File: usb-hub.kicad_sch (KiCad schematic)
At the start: 15 parts, among them U302 CH334P, Y900 12Mhz

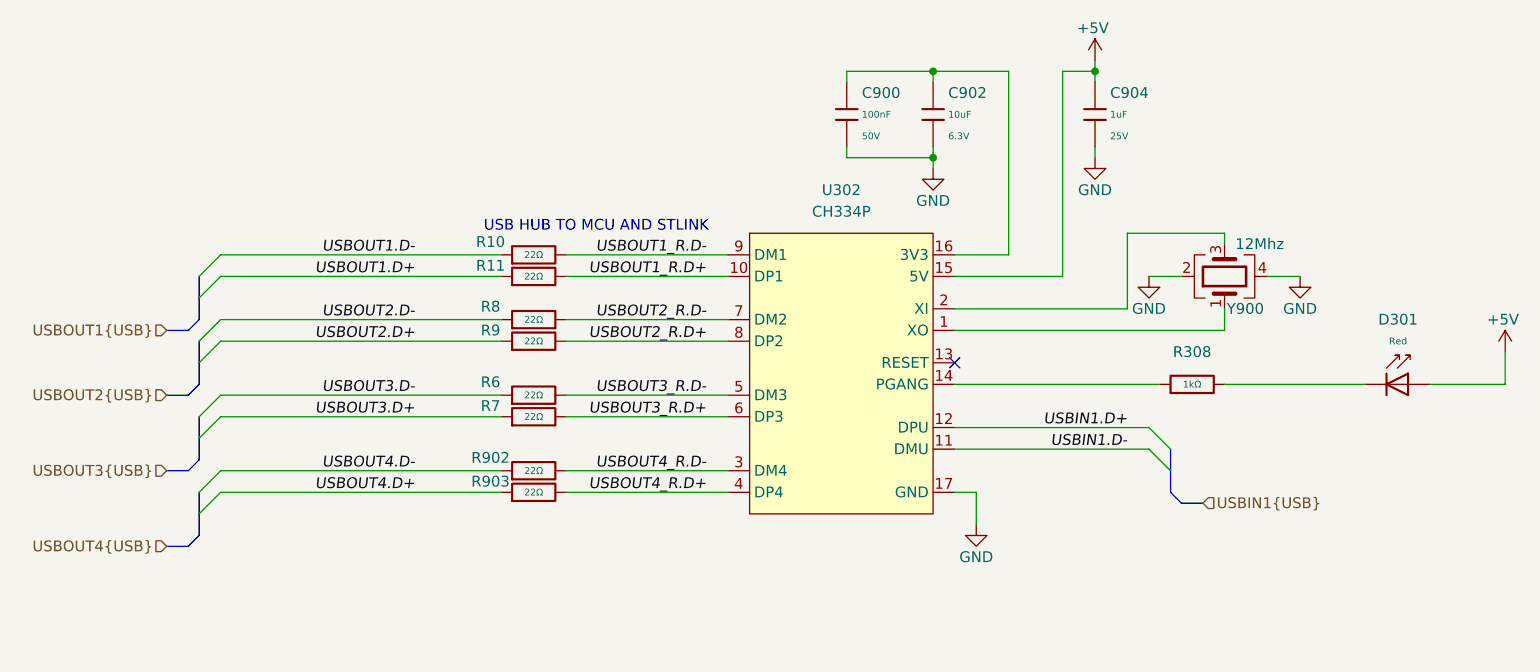
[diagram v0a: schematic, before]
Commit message: [#1] WIP: Change components to ones from the global library, refactor schematic
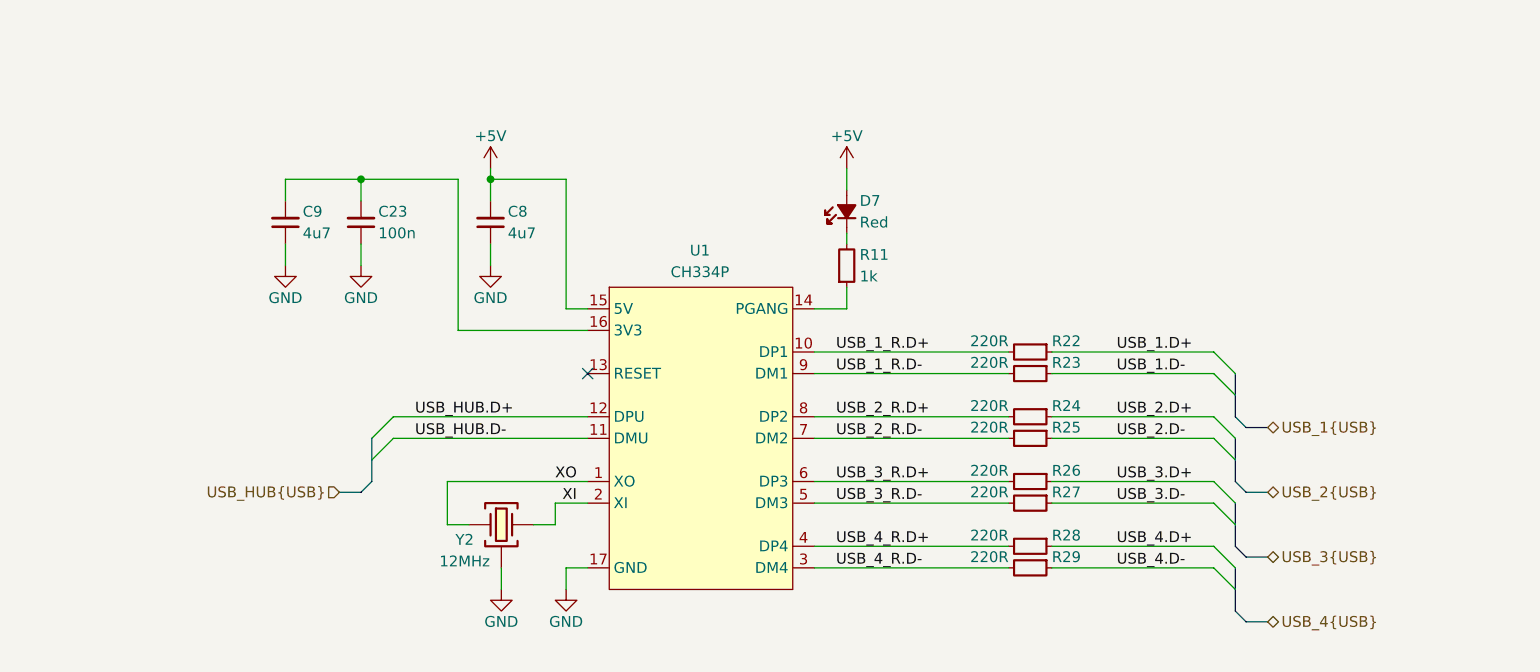
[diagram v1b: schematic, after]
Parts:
- removed C900: 100nF, PCM_JLCPCB:C_0402, symbol PCM_JLCPCB-Capacitors:0402,100nF,(2)
- removed C902: 10uF, PCM_JLCPCB:C_0402, symbol PCM_JLCPCB-Capacitors:0402,10uF
- removed C904: 1uF, PCM_JLCPCB:C_0402, symbol PCM_JLCPCB-Capacitors:0402,1uF
- removed D301: Red, PCM_JLCPCB:D_0603, symbol PCM_JLCPCB-Diodes:LED,0603,Red
- removed R10, R11, R6, R7, R8, R9, R902, R903: 22Ω, PCM_JLCPCB:R_0402, symbol PCM_JLCPCB-Resistors:0402,22Ω
- removed R308: 1kΩ, PCM_JLCPCB:R_0402, symbol PCM_JLCPCB-Resistors:0402,1kΩ
- removed U302: CH334P, Package_DFN_QFN:QFN-16-1EP_3x3mm_P0.5mm_EP1.7x1.7mm, symbol CH334P:CH334P
- removed Y900: 12Mhz, Crystal:Crystal_SMD_3225-4Pin_3.2x2.5mm, symbol Device:Crystal_GND24
- added C23: C-100n-0402, DW-footprints:C_0402_1005Metric, symbol DW-capacitors:C-100n-0402
- added C8, C9: C-4u7-0402, DW-footprints:C_0402_1005Metric, symbol DW-capacitors:C-4u7-0402
- added D7: LED-R-0603_KT-0603R, DW-footprints:LED_0603_1608Metric_R, symbol DW-diodes:LED-R-0603_KT-0603R
- added R11: R-1k-0402, DW-footprints:R_0402_1005Metric, symbol DW-resistors:R-1k-0402
- added R22, R23, R24, R25, R26, R27, R28, R29: R-220r-0402, DW-footprints:R_0402_1005Metric, symbol DW-resistors:R-220r-0402
- added U1: CH334P, DW-footprints:QFN-16-1EP_3x3mm_P0.5mm_EP1.75x1.75mm, symbol DW-ICs:CH334P
- added Y2: X322512MSB4SI, DW-footprints:Crystal_SMD_3225-4Pin_3.2x2.5mm, symbol DW-crystals:Crystal_12MHz_X322512MSB4SI
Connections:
- net +5V: now also C8.2, D7.2 (A), U1.15 (5V)
- net GND: now also C23.1, C8.1, C9.1, U1.17 (GND), Y2.2 (SH), Y2.4 (SH)
- new net: D7.1 (C), R11.2
- new net: R11.1, U1.14 (PGANG)
- new net: C23.2, C9.2, U1.16 (3V3)
- new net USB_1.D+: R22.1
- new net USB_1.D-: R23.1
- new net USB_1_R.D+: R22.2, U1.10 (DP1)
- new net USB_1_R.D-: R23.2, U1.9 (DM1)
- new net USB_2.D+: R24.1
- new net USB_2.D-: R25.1
- new net USB_2_R.D+: R24.2, U1.8 (DP2)
- new net USB_2_R.D-: R25.2, U1.7 (DM2)
- new net USB_3.D+: R26.1
- new net USB_3.D-: R27.1
- new net USB_3_R.D+: R26.2, U1.6 (DP3)
- new net USB_3_R.D-: R27.2, U1.5 (DM3)
- new net USB_4.D+: R28.1
- new net USB_4.D-: R29.1
- new net USB_4_R.D+: R28.2, U1.4 (DP4)
- new net USB_4_R.D-: R29.2, U1.3 (DM4)
- new net USB_HUB.D+: U1.12 (DPU)
- new net USB_HUB.D-: U1.11 (DMU)
- new net XI: U1.2 (XI), Y2.3
- new net XO: U1.1 (XO), Y2.1
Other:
- note removed: "USB HUB TO MCU AND STLINK"

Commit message: [#1] Re-annotate schematic
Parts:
- renumbered C9 to C21, C23 to C22, C8 to C23, D7 to D8, R11 to R26, R22 to R27, R23 to R28, R24 to R29, R25 to R30, R26 to R31, R27 to R32, R28 to R33, R29 to R34, U1 to U5
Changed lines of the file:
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@@
 		(on_board yes)
 		(dnp no)
-		(property "Reference" "D7"
+		(property "Reference" "D8"
 			(at 152.654 77.47 90)
 			(effects
@@
 			(project "cm5-module"
 				(path "/090a8e41-87a8-4fb1-998b-60a2c0dc4cee/4f95f4d3-6409-4bd0-9a25-1272a43f6549"
-					(reference "D7")
+					(reference "D8")
 					(unit 1)
 				)
@@
 		(on_board yes)
 		(dnp no)
-		(property "Reference" "U1"
+		(property "Reference" "U5"
 			(at 133.858 83.312 0)
 			(effects
@@
 			(project ""
 				(path "/090a8e41-87a8-4fb1-998b-60a2c0dc4cee/4f95f4d3-6409-4bd0-9a25-1272a43f6549"
-					(reference "U1")
+					(reference "U5")
 					(unit 1)
 				)
@@
 		(on_board yes)
 		(dnp no)
-		(property "Reference" "R24"
+		(property "Reference" "R29"
 			(at 175.26 101.6 0)
 			(effects
@@
 			(project "cm5-module"
 				(path "/090a8e41-87a8-4fb1-998b-60a2c0dc4cee/4f95f4d3-6409-4bd0-9a25-1272a43f6549"
-					(reference "R24")
+					(reference "R29")
 					(unit 1)
 				)
@@
 		(on_board yes)
 		(dnp no)
-		(property "Reference" "#PWR062"
+		(property "Reference" "#PWR070"
 			(at 85.09 91.44 0)
 			(effects
@@
 			(project "cm5-module"
 				(path "/090a8e41-87a8-4fb1-998b-60a2c0dc4cee/4f95f4d3-6409-4bd0-9a25-1272a43f6549"
-					(reference "#PWR062")
+					(reference "#PWR070")
 					(unit 1)
 				)
@@
 		(on_board yes)
 		(dnp no)
-		(property "Reference" "#PWR058"
+		(property "Reference" "#PWR073"
 			(at 110.49 129.54 0)
 			(effects
@@
 			(project "cm5-module"
 				(path "/090a8e41-87a8-4fb1-998b-60a2c0dc4cee/4f95f4d3-6409-4bd0-9a25-1272a43f6549"
-					(reference "#PWR058")
+					(reference "#PWR073")
 					(unit 1)
 				)
@@
 		(on_board yes)
 		(dnp no)
-		(property "Reference" "#PWR059"
+		(property "Reference" "#PWR071"
 			(at 93.98 91.44 0)
 			(effects
@@
 			(project "cm5-module"
 				(path "/090a8e41-87a8-4fb1-998b-60a2c0dc4cee/4f95f4d3-6409-4bd0-9a25-1272a43f6549"
-					(reference "#PWR059")
+					(reference "#PWR071")
 					(unit 1)
 				)
@@
 		(on_board yes)
 		(dnp no)
-		(property "Reference" "#PWR049"
+		(property "Reference" "#PWR074"
 			(at 118.11 129.54 0)
 			(effects
@@
 			(project "cm5-module"
 				(path "/090a8e41-87a8-4fb1-998b-60a2c0dc4cee/4f95f4d3-6409-4bd0-9a25-1272a43f6549"
-					(reference "#PWR049")
+					(reference "#PWR074")
 					(unit 1)
 				)
@@
 		(on_board yes)
 		(dnp no)
-		(property "Reference" "R23"
+		(property "Reference" "R28"
 			(at 175.26 96.52 0)
 			(effects
@@
 			(project "cm5-module"
 				(path "/090a8e41-87a8-4fb1-998b-60a2c0dc4cee/4f95f4d3-6409-4bd0-9a25-1272a43f6549"
-					(reference "R23")
+					(reference "R28")
 					(unit 1)
 				)
@@
 		(on_board yes)
 		(dnp no)
-		(property "Reference" "R11"
+		(property "Reference" "R26"
 			(at 152.654 83.82 90)
 			(effects
@@
 			(project "cm5-module"
 				(path "/090a8e41-87a8-4fb1-998b-60a2c0dc4cee/4f95f4d3-6409-4bd0-9a25-1272a43f6549"
-					(reference "R11")
+					(reference "R26")
 					(unit 1)
 				)
@@
 		(on_board yes)
 		(dnp no)
-		(property "Reference" "R28"
+		(property "Reference" "R33"
 			(at 175.26 116.84 0)
 			(effects
@@
 			(project "cm5-module"
 				(path "/090a8e41-87a8-4fb1-998b-60a2c0dc4cee/4f95f4d3-6409-4bd0-9a25-1272a43f6549"
-					(reference "R28")
+					(reference "R33")
 					(unit 1)
 				)
@@
 		(on_board yes)
 		(dnp no)
-		(property "Reference" "R22"
+		(property "Reference" "R27"
 			(at 175.26 93.98 0)
 			(effects
@@
 			(project "cm5-module"
 				(path "/090a8e41-87a8-4fb1-998b-60a2c0dc4cee/4f95f4d3-6409-4bd0-9a25-1272a43f6549"
-					(reference "R22")
+					(reference "R27")
 					(unit 1)
 				)
@@
 		(on_board yes)
 		(dnp no)
-		(property "Reference" "R26"
+		(property "Reference" "R31"
 			(at 175.26 109.22 0)
 			(effects
@@
 			(project "cm5-module"
 				(path "/090a8e41-87a8-4fb1-998b-60a2c0dc4cee/4f95f4d3-6409-4bd0-9a25-1272a43f6549"
-					(reference "R26")
+					(reference "R31")
 					(unit 1)
 				)
@@
 		(on_board yes)
 		(dnp no)
-		(property "Reference" "C23"
+		(property "Reference" "C22"
 			(at 96.012 78.74 90)
 			(effects
@@
 			(project "cm5-module"
 				(path "/090a8e41-87a8-4fb1-998b-60a2c0dc4cee/4f95f4d3-6409-4bd0-9a25-1272a43f6549"
-					(reference "C23")
+					(reference "C22")
 					(unit 1)
 				)
@@
 		(on_board yes)
 		(dnp no)
-		(property "Reference" "C8"
+		(property "Reference" "C23"
 			(at 111.252 78.74 90)
 			(effects
@@
 			(project ""
 				(path "/090a8e41-87a8-4fb1-998b-60a2c0dc4cee/4f95f4d3-6409-4bd0-9a25-1272a43f6549"
-					(reference "C8")
+					(reference "C23")
 					(unit 1)
 				)
@@
 		(on_board yes)
 		(dnp no)
-		(property "Reference" "C9"
+		(property "Reference" "C21"
 			(at 87.122 78.74 90)
 			(effects
@@
 			(project "cm5-module"
 				(path "/090a8e41-87a8-4fb1-998b-60a2c0dc4cee/4f95f4d3-6409-4bd0-9a25-1272a43f6549"
-					(reference "C9")
+					(reference "C21")
 					(unit 1)
 				)
@@
 		(on_board yes)
 		(dnp no)
-		(property "Reference" "R25"
+		(property "Reference" "R30"
 			(at 175.26 104.14 0)
 			(effects
@@
 			(project "cm5-module"
 				(path "/090a8e41-87a8-4fb1-998b-60a2c0dc4cee/4f95f4d3-6409-4bd0-9a25-1272a43f6549"
-					(reference "R25")
+					(reference "R30")
 					(unit 1)
 				)
@@
 		(on_board yes)
 		(dnp no)
-		(property "Reference" "#PWR042"
+		(property "Reference" "#PWR069"
 			(at 151.13 77.47 0)
 			(effects
@@
 			(project "cm5-module"
 				(path "/090a8e41-87a8-4fb1-998b-60a2c0dc4cee/4f95f4d3-6409-4bd0-9a25-1272a43f6549"
-					(reference "#PWR042")
+					(reference "#PWR069")
 					(unit 1)
 				)
@@
 		(on_board yes)
 		(dnp no)
-		(property "Reference" "R27"
+		(property "Reference" "R32"
 			(at 175.26 111.76 0)
 			(effects
@@
 			(project "cm5-module"
 				(path "/090a8e41-87a8-4fb1-998b-60a2c0dc4cee/4f95f4d3-6409-4bd0-9a25-1272a43f6549"
-					(reference "R27")
+					(reference "R32")
 					(unit 1)
 				)
@@
 		(on_board yes)
 		(dnp no)
-		(property "Reference" "R29"
+		(property "Reference" "R34"
 			(at 175.26 119.38 0)
 			(effects
@@
 			(project "cm5-module"
 				(path "/090a8e41-87a8-4fb1-998b-60a2c0dc4cee/4f95f4d3-6409-4bd0-9a25-1272a43f6549"
-					(reference "R29")
+					(reference "R34")
 					(unit 1)
 				)
@@
 		(on_board yes)
 		(dnp no)
-		(property "Reference" "#PWR034"
+		(property "Reference" "#PWR068"
 			(at 109.22 77.47 0)
 			(effects
@@
 			(project "cm5-module"
 				(path "/090a8e41-87a8-4fb1-998b-60a2c0dc4cee/4f95f4d3-6409-4bd0-9a25-1272a43f6549"
-					(reference "#PWR034")
+					(reference "#PWR068")
 					(unit 1)
 				)
@@
 		(on_board yes)
 		(dnp no)
-		(property "Reference" "#PWR047"
+		(property "Reference" "#PWR072"
 			(at 109.22 91.44 0)
 			(effects
@@
 			(project "cm5-module"
 				(path "/090a8e41-87a8-4fb1-998b-60a2c0dc4cee/4f95f4d3-6409-4bd0-9a25-1272a43f6549"
-					(reference "#PWR047")
+					(reference "#PWR072")
 					(unit 1)
 				)

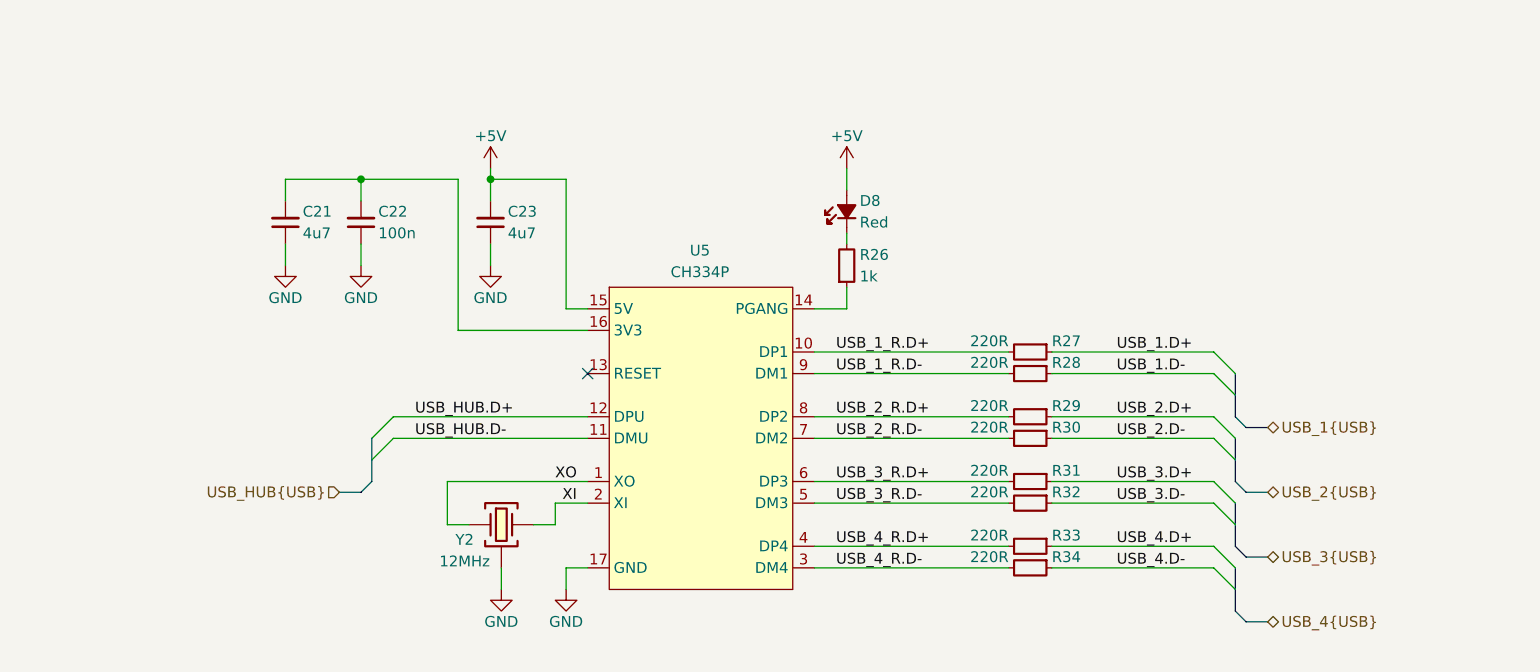
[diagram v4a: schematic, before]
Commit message: [#1] WIP: Refactor schematic
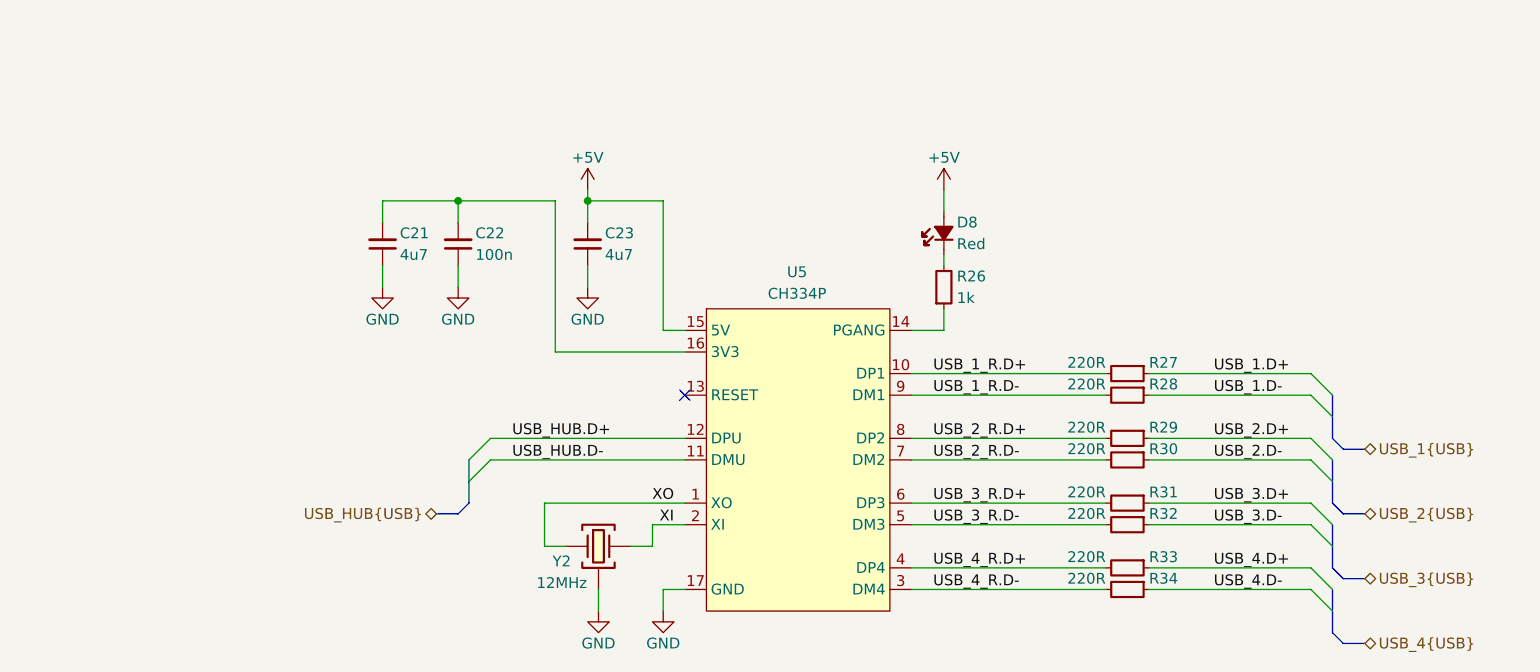
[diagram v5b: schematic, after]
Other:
- moved on the sheet: C21, C22, C23, D8, R26, R27, R28, R29, R30, R31, R32, R33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

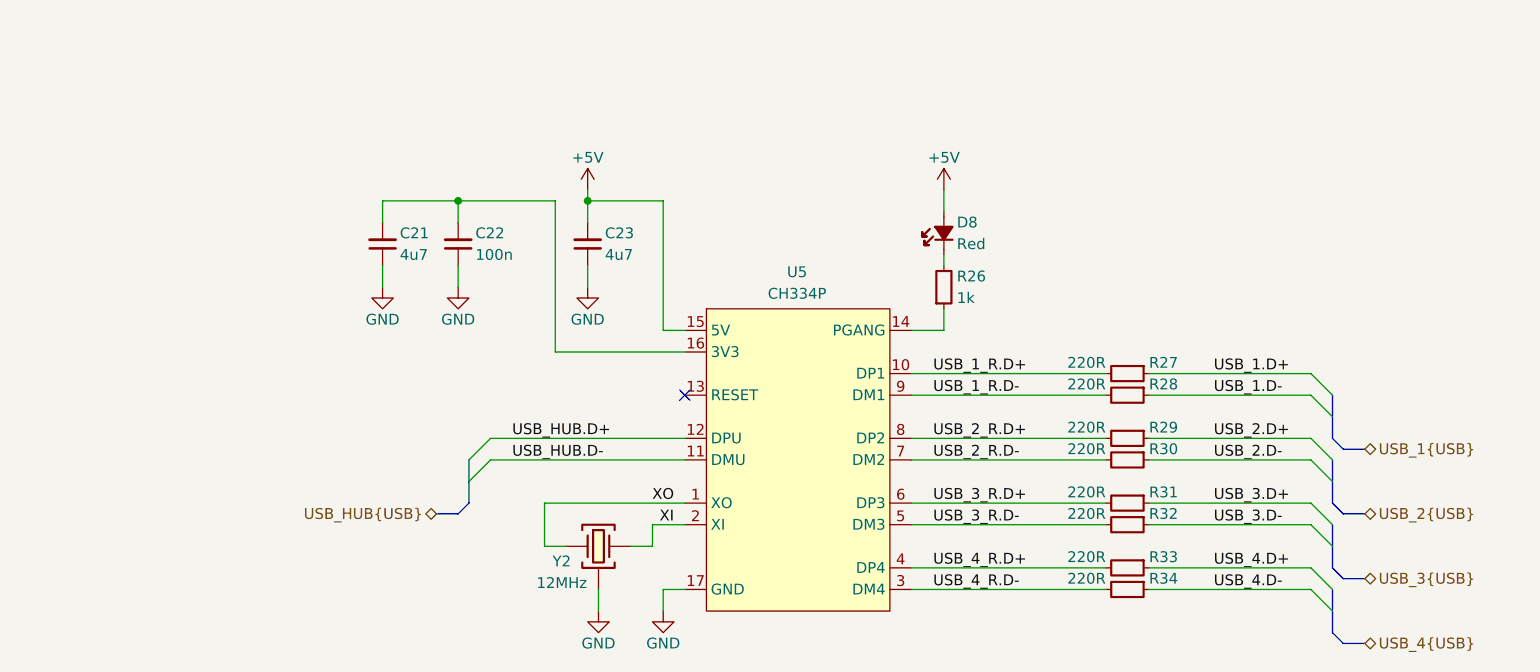
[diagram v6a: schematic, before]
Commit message: [#1] Add USB switch and 0R to USB hub data lines, minor schematic refactor
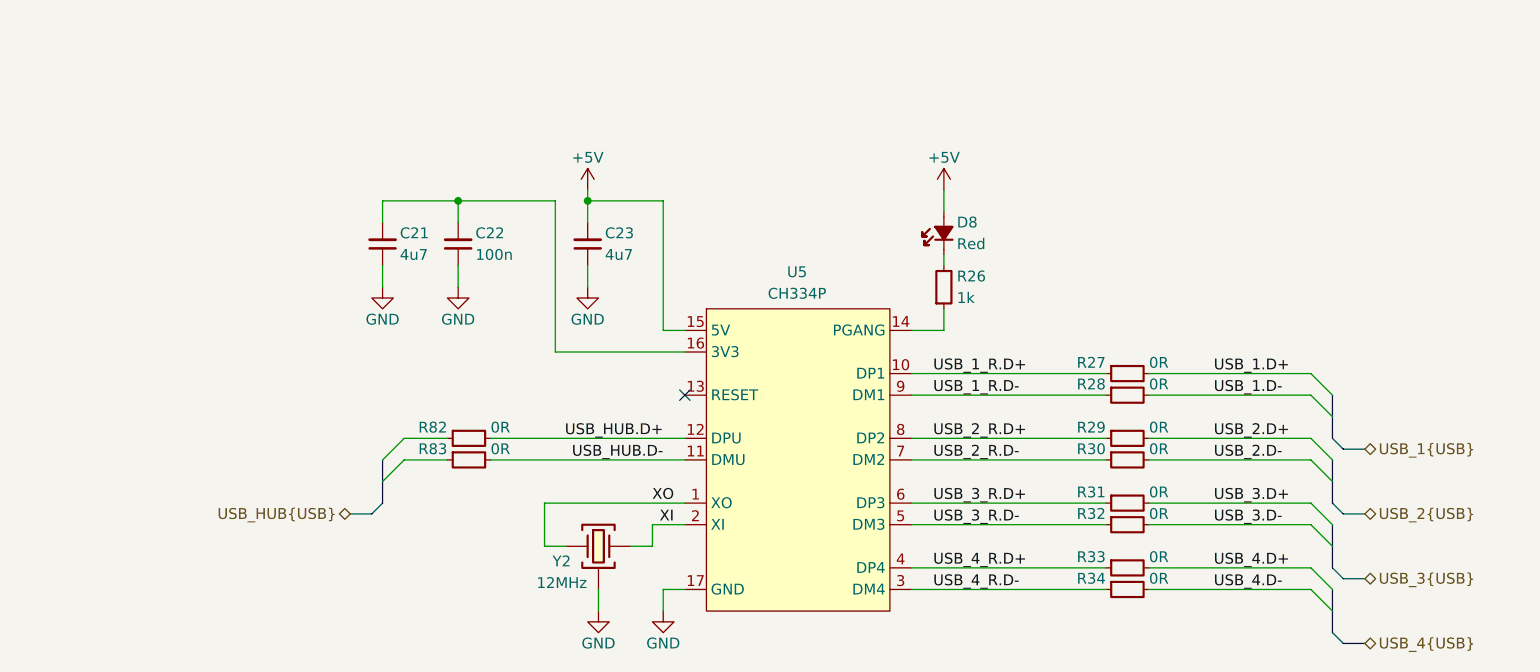
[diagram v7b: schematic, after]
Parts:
- removed R27, R28, R29, R30, R31, R32, R33, R34: R-220r-0402, DW-footprints:R_0402_1005Metric, symbol DW-resistors:R-220r-0402
- added R27, R28, R29, R30, R31, R32, R33, R34, R82, R83: R-0R-0402, DW-footprints:R_0402_1005Metric, symbol DW-resistors:R-0R-0402
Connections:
- net USB_1.D+: now also R27.2
- net USB_1.D-: now also R28.2
- net USB_1_R.D+: now also R27.1
- net USB_1_R.D-: now also R28.1
- net USB_2.D+: now also R29.2
- net USB_2.D-: now also R30.2
- net USB_2_R.D+: now also R29.1
- net USB_2_R.D-: now also R30.1
- net USB_3.D+: now also R31.2
- net USB_3.D-: now also R32.2
- net USB_3_R.D+: now also R31.1
- net USB_3_R.D-: now also R32.1
- net USB_4.D+: now also R33.2
- net USB_4.D-: now also R34.2
- net USB_4_R.D+: now also R33.1
- net USB_4_R.D-: now also R34.1
- net USB_HUB.D+: now also R82.2
- net USB_HUB.D-: now also R83.2
